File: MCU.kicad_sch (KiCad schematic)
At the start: 27 parts, among them J1 Conn_ARM_SWD_TagConnect_TC2030, U1 W25Q128JVP, U2 STM32WB55CGUx, U3 MLPF-WB55-01E3, X1 32MHz, X2 32kHz768

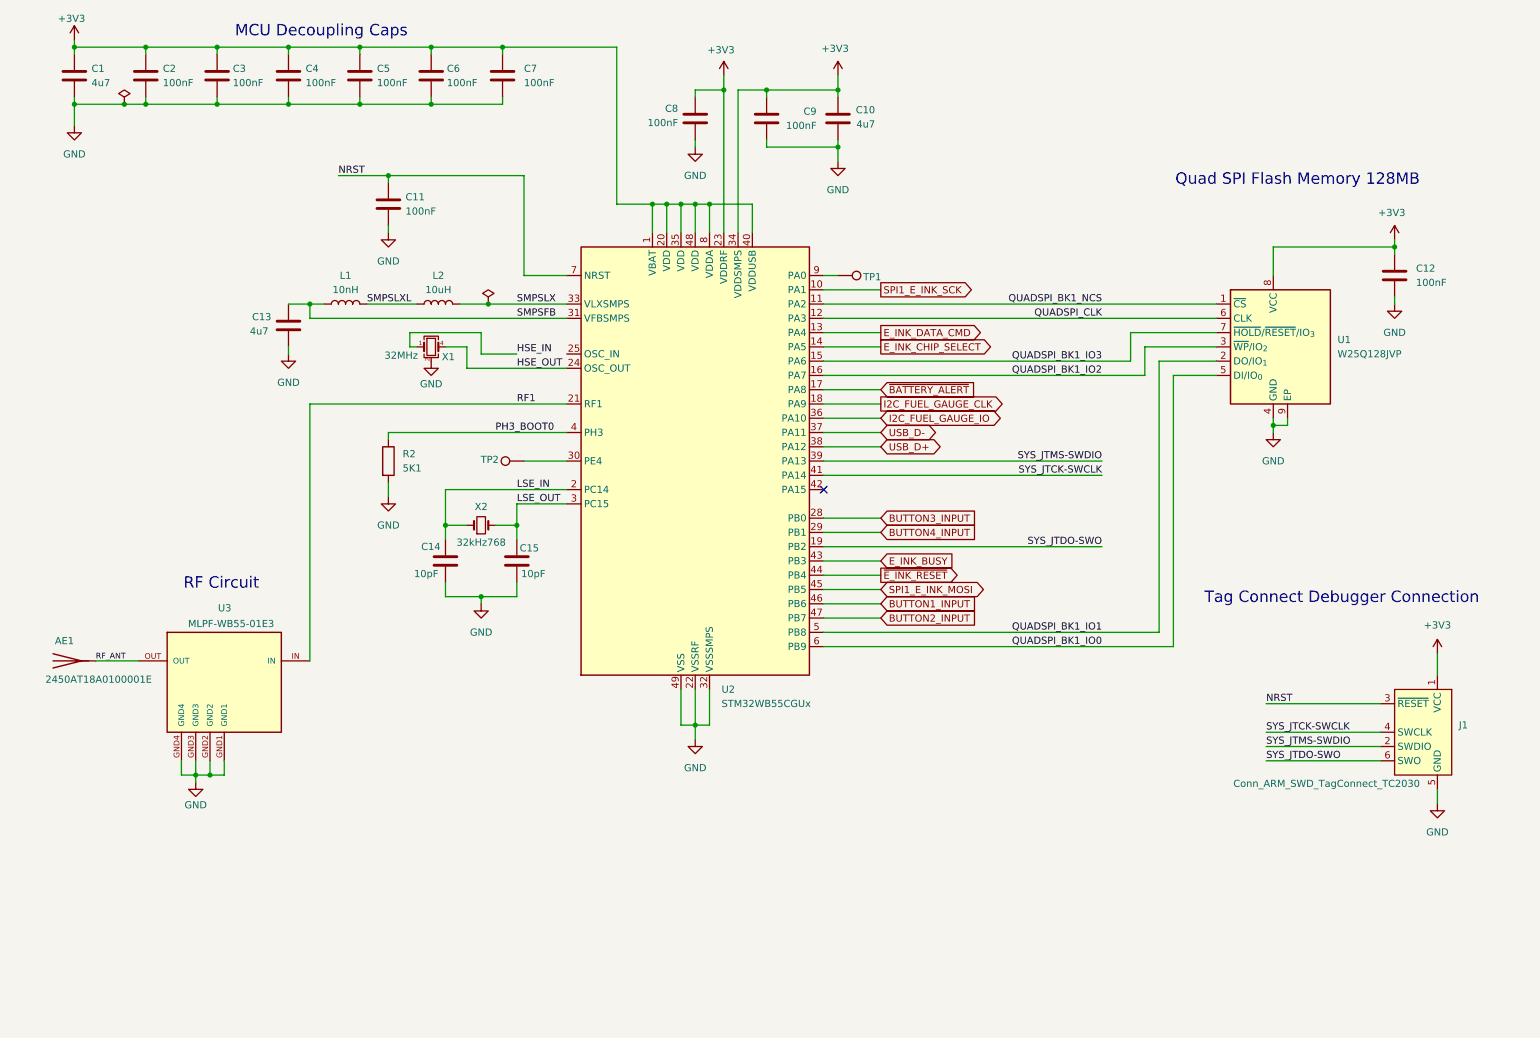
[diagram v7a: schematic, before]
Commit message: Changed from stm32wb -> nRF52 module
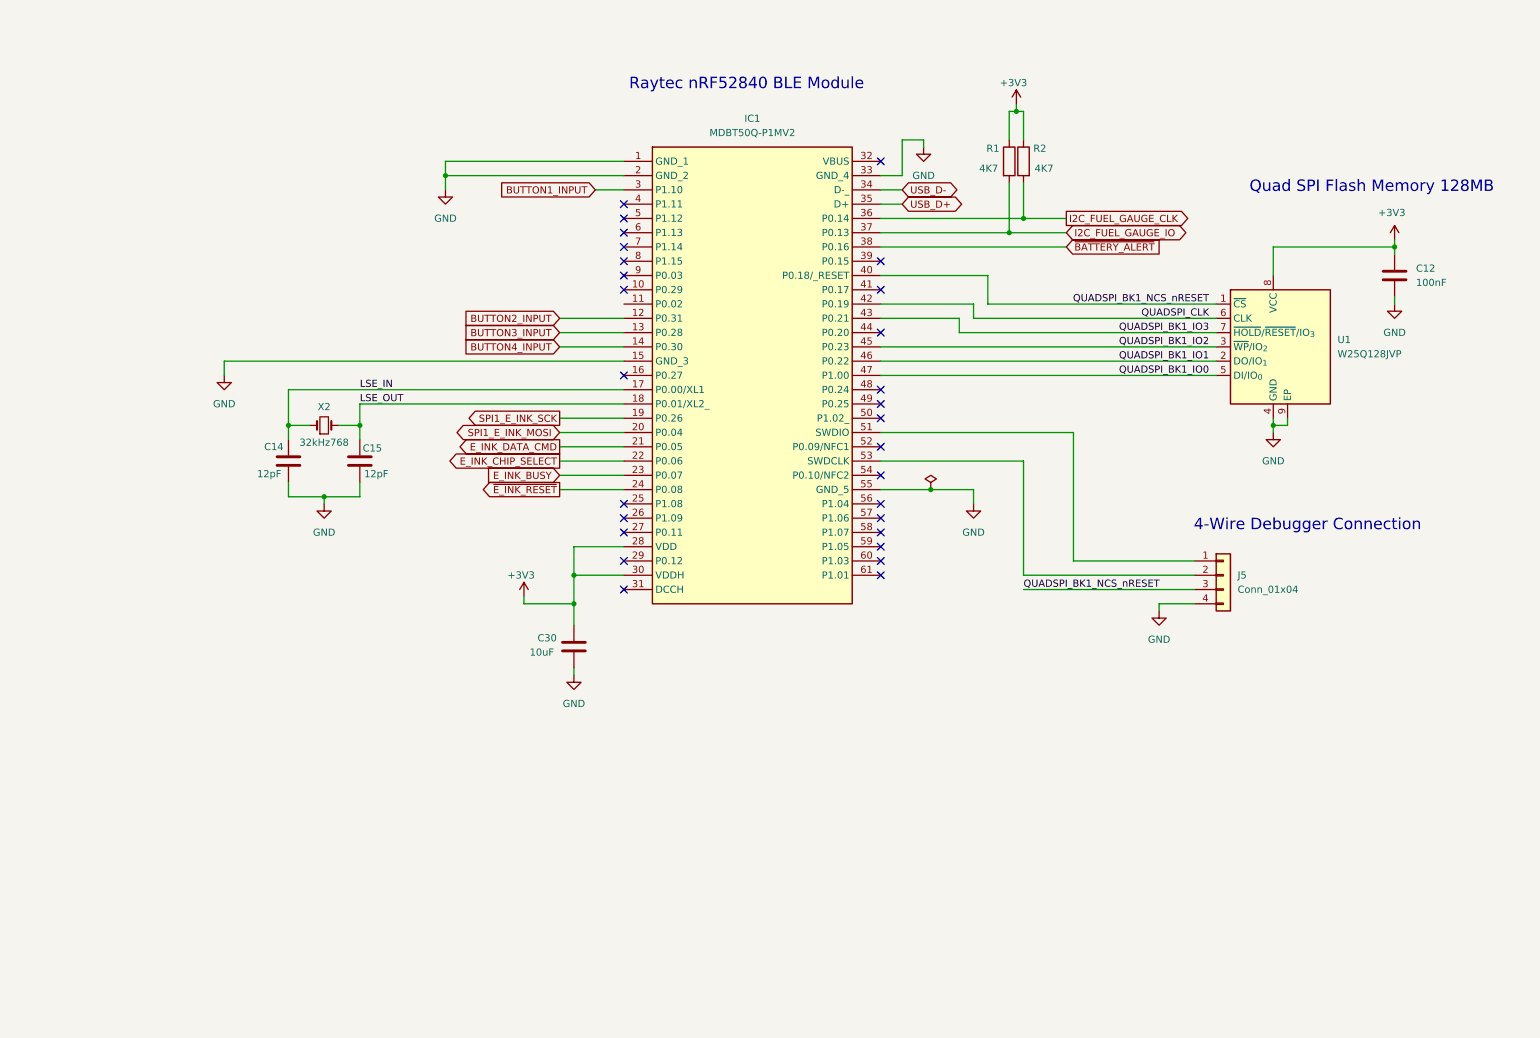
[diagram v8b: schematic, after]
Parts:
- removed AE1: 2450AT18A0100001E, LibraryFootprints:XCVR_2450AT18A0100001E, symbol Device:Antenna
- removed C1, C10, C13: 4u7, Capacitor_SMD:C_0603_1608Metric, symbol Device:C
- removed C11, C2, C3, C4, C5, C6, C7, C8, C9: 100nF, Capacitor_SMD:C_0402_1005Metric, symbol Device:C
- removed J1: Conn_ARM_SWD_TagConnect_TC2030, Connector:Tag-Connect_TC2030-IDC-FP_2x03_P1.27mm_Vertical, symbol Connector:Conn_ARM_SWD_TagConnect_TC2030
- removed L1: 10nH, Inductor_SMD:L_0402_1005Metric, symbol Device:L
- removed L2: 10uH, Inductor_SMD:L_0805_2012Metric, symbol Device:L
- removed TP1, TP2: ~, TestPoint:TestPoint_Pad_D1.0mm, symbol Connector:TestPoint
- removed U2: STM32WB55CGUx, Package_DFN_QFN:QFN-48-1EP_7x7mm_P0.5mm_EP5.6x5.6mm, symbol MCU_ST_STM32WB:STM32WB55CGUx
- removed U3: MLPF-WB55-01E3, LibraryFootprints:MLPF-WB55-01E3, symbol MLPF-WB55-01E3:MLPF-WB55-01E3
- removed X1: 32MHz, Crystal:Crystal_SMD_2016-4Pin_2.0x1.6mm, symbol Device:Crystal_GND23_Small
- added C30: 10uF, Capacitor_SMD:C_0603_1608Metric, symbol Device:C
- added IC1: MDBT50Q-P1MV2, LibraryFootprints:MDBT50QP1MV2, symbol MCU_Module:MDBT50Q-P1MV2
- added J5: Conn_01x04, Connector_PinHeader_2.54mm:PinHeader_1x04_P2.54mm_Vertical, symbol Connector_Generic:Conn_01x04
- added R1: 4K7, Resistor_SMD:R_0402_1005Metric, symbol Device:R
- C14, C15: value 10pF -> 12pF
- R2: value 5K1 -> 4K7
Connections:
- net PH3_BOOT0 is gone; now on net +3V3: R2.1
- net +3V3: now also C30.1, IC1.28 (VDD), IC1.30 (VDDH), R1.1
- net BUTTON1_INPUT: now also IC1.3 (P1.10)
- net BUTTON2_INPUT: now also IC1.12 (P0.31)
- net BUTTON3_INPUT: now also IC1.13 (P0.28)
- net BUTTON4_INPUT: now also IC1.14 (P0.30)
- net E_INK_BUSY: now also IC1.23 (P0.07)
- net E_INK_CHIP_SELECT: now also IC1.22 (P0.06)
- net E_INK_DATA_CMD: now also IC1.21 (P0.05)
- net GND: now also C30.2, IC1.1 (GND_1), IC1.15 (GND_3), IC1.2 (GND_2), IC1.33 (GND_4), IC1.55 (GND_5), J5.4 (Pin_4); no longer R2.2
- net I2C_FUEL_GAUGE_CLK: now also R2.2, IC1.36 (P0.14)
- net I2C_FUEL_GAUGE_IO: now also IC1.37 (P0.13), R1.2
- net LSE_IN: now also IC1.17 (P0.00/XL1)
- net LSE_OUT: now also IC1.18 (P0.01/XL2_)
- net QUADSPI_BK1_IO0: now also IC1.47 (P1.00)
- net QUADSPI_BK1_IO1: now also IC1.46 (P0.22)
- net QUADSPI_BK1_IO2: now also IC1.45 (P0.23)
- net QUADSPI_BK1_IO3: now also IC1.43 (P0.21)
- net QUADSPI_CLK: now also IC1.42 (P0.19)
- net SPI1_E_INK_MOSI: now also IC1.20 (P0.04)
- net SPI1_E_INK_SCK: now also IC1.19 (P0.26)
- net USB_D+: now also IC1.35 (D+)
- net USB_D-: now also IC1.34 (D˗_)
- net ~{BATTERY_ALERT}: now also IC1.38 (P0.16)
- net ~{E_INK_RESET}: now also IC1.24 (P0.08)
- net QUADSPI_BK1_NCS renamed QUADSPI_BK1_NCS_nRESET
- net QUADSPI_BK1_NCS_nRESET: now also IC1.40 (P0.18/_RESET), J5.3 (Pin_3)
- new net: IC1.51 (SWDIO), J5.1 (Pin_1)
- new net: IC1.53 (SWDCLK), J5.2 (Pin_2)
- no-connect marks 1 -> 28
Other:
- note added: "4-Wire Debugger Connection"
- note added: "Raytec nRF52840 BLE Module"
- note removed: "MCU Decoupling Caps"
- note removed: "RF Circuit"
- note removed: "Tag Connect Debugger Connection"
- moved on the sheet: C14, C15, X2
